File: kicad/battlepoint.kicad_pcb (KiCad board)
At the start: 2 copper layers, 13 parts, among them J1 Arduino1, J2 Arduino2, J3 Arduino3, J4 Arduino4, J5 PANEL, J6 SWITCHES, J7 Barrel_Jack, J8 LIGHTS, U1 LM7805_TO220

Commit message: working mostly
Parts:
- removed C1: 0.1uf, Capacitors_THT:C_Rect_L7.0mm_W2.5mm_P5.00mm
- removed C2: 22uf, Capacitors_THT:CP_Radial_D4.0mm_P1.50mm
- removed J2: Arduino2, Socket_Strips:Socket_Strip_Straight_1x06_Pitch2.54mm
- removed J3: Arduino3, Socket_Strips:Socket_Strip_Straight_1x08_Pitch2.54mm
- removed J4: Arduino4, Socket_Strips:Socket_Strip_Straight_1x08_Pitch2.54mm
- removed J5: PANEL, Connectors:RJ45_8
- removed J6: SWITCHES, Connectors:RJ45_8
- removed J7: Barrel_Jack, Connectors:BARREL_JACK
- removed J8: LIGHTS, Connectors:RJ45_8
- added ARD1: UNO_SHIELD, Arduino:Arduino_Uno_Shield, F.Cu at (87.6, 188.0)
- added P1: TMR1_LED, Connect:USB_A, F.Cu at (74.9, 99.1)
- added P10: OLED, Connectors_JST:JST_XH_B04B-XH-A_04x2.50mm_Straight, F.Cu at (47.0, 143.5)
- added P2: TMR2_LED, Connect:USB_A, F.Cu at (40.6, 99.1)
- added P3: CAP_LED, Connect:USB_A, F.Cu at (58.4, 99.1)
- added P4: OWN_LED, Connect:USB_A, F.Cu at (91.4, 99.1)
- added P5: SPK, Connectors_JST:JST_XH_B02B-XH-A_02x2.50mm_Straight, F.Cu at (68.6, 130.8)
- added P8: AUDIO_JACK, Connectors_JST:JST_XH_B04B-XH-A_04x2.50mm_Straight, F.Cu at (47.0, 129.5)
- added P9: KEYPAD, Connectors_JST:JST_XH_B03B-XH-A_03x2.50mm_Straight, F.Cu at (63.5, 143.5)
- J1: value Arduino1 -> BTNS; footprint Socket_Strips:Socket_Strip_Straight_1x06_Pitch2.54mm -> Connect:RJ45_8
- R1, R2: footprint Resistors_THT:R_Axial_DIN0204_L3.6mm_D1.6mm_P2.54mm_Vertical -> Resistors_ThroughHole:Resistor_Horizontal_RM7mm
- U1: value LM7805_TO220 -> DFPLAYER_MINI; footprint TO_SOT_Packages_THT:TO-220-3_Vertical -> Arduino:dfplayer_mini
- moved R2 77.2 mm to (80.0, 149.9)
- moved U1 74.7 mm to (45.7, 156.2)
- moved R1 72.9 mm to (80.0, 137.2)
- moved J1 55.7 mm to (41.9, 110.5), turned to 90 degrees
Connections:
- J1 pad 1: A5 -> GND
- J1 pad 2: A4 -> +5V
- J1 pad 3: A3 -> D2
- J1 pad 4: A2 -> D11
- J1 pad 5: A1 -> GND
- J1 pad 6: A0 -> +5V
- R1 pad 1: +VDC -> Net-(ARD1-PadVIN)
- R1 pad 2: A2 -> A4
- R2 pad 1: A2 -> A4
- R2 pad 2: Net-(J7-Pad2) -> GND
- U1 pad 1: +VDC -> +5V
- U1 pad 2: GND -> D8
- U1 pad 3: +5V -> D9
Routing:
- net A2: track 112.0 -> 0.00 mm
- net GND: track 91.9 -> 0.00 mm
- net A0: track 44.5 -> 0.00 mm
- net P3: track 36.2 -> 0.00 mm
- net +VDC: track 32.6 -> 0.00 mm
- net P5: track 32.1 -> 0.00 mm
- net +5V: track 31.8 -> 0.00 mm
- net P6: track 31.3 -> 0.00 mm
- net A4: track 18.1 -> 0.00 mm
- net A5: track 12.5 -> 0.00 mm
- net Net-(J7-Pad2): track 9.03 -> 0.00 mm
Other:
- board outline added: 77.5 x 100.3 mm
- net class PWR removed

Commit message: progress
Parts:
- removed P10: OLED, Connectors_JST:JST_XH_B04B-XH-A_04x2.50mm_Straight
- removed P9: KEYPAD, Connectors_JST:JST_XH_B03B-XH-A_03x2.50mm_Straight
- added P12: PANEL_OUT, Connectors_JST:JST_XH_B05B-XH-A_05x2.50mm_Straight, F.Cu at (109.2, 184.2)
- added P13: PANEL_IN, Connectors_JST:JST_XH_B05B-XH-A_05x2.50mm_Straight, F.Cu at (66.0, 100.3)
- added P14: OLED_OUT, Connectors_JST:JST_XH_B04B-XH-A_04x2.50mm_Straight, F.Cu at (91.4, 95.2)
- added R3: 2K, Resistors_ThroughHole:Resistor_Horizontal_RM7mm, F.Cu at (26.7, 92.7)
- added R4: 330, Resistors_ThroughHole:Resistor_Horizontal_RM7mm, F.Cu at (39.4, 92.7)
- added R5: 620, Resistors_ThroughHole:Resistor_Horizontal_RM7mm, F.Cu at (52.1, 92.7)
- added R6: 1K, Resistors_ThroughHole:Resistor_Horizontal_RM7mm, F.Cu at (63.5, 92.7)
- added R7: 3.3K, Resistors_ThroughHole:Resistor_Horizontal_RM7mm, F.Cu at (74.9, 92.7)
- added SW1: BTN_UP, Buttons_Switches_ThroughHole:SW_PUSH_6mm, B.Cu at (26.7, 97.8)
- added SW2: BTN_DWN, Buttons_Switches_ThroughHole:SW_PUSH_6mm, B.Cu at (39.4, 97.8)
- added SW3: BTN_SEL, Buttons_Switches_ThroughHole:SW_PUSH_6mm, B.Cu at (52.1, 97.8)
- moved P8 71.7 mm to (109.2, 165.1), turned to 90 degrees
- moved J1 63.7 mm to (105.4, 115.6), turned to 180 degrees
- moved P2 55.2 mm to (91.4, 120.7)
- moved P5 45.8 mm to (101.6, 162.6), turned to 270 degrees
- moved P3 30.5 mm to (36.8, 120.7)
- moved P1 28.8 mm to (55.9, 120.7)
- moved P4 28.0 mm to (73.7, 120.7)
- moved U1 15.2 mm to (45.7, 171.4)
- moved R1 13.7 mm to (87.6, 148.6)
- moved R2 11.7 mm to (87.6, 158.8)
- moved ARD1 8.13 mm to (82.5, 194.3)
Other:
- board size 77.5 x 100.3 mm -> 101.6 x 153.7 mm

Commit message: about to start routing
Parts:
- R3, R4, R5, R6, R7: footprint Resistors_ThroughHole:Resistor_Horizontal_RM7mm -> Resistors_ThroughHole:Resistor_Vertical_RM5mm
- moved P12 39.4 mm to (109.2, 144.8)
- moved P14 38.9 mm to (53.3, 102.9), turned to 180 degrees
- moved R3 36.1 mm to (61.0, 104.1), turned to 180 degrees
- moved P13 28.1 mm to (38.1, 102.9), turned to 180 degrees
- moved U1 25.7 mm to (59.7, 149.9)
- moved R4 22.9 mm to (61.0, 100.3), turned to 180 degrees
- moved R7 14.5 mm to (61.0, 88.9), turned to 180 degrees
- moved ARD1 14.0 mm to (96.5, 194.3)
- moved P5 14.0 mm to (101.6, 176.5)
- moved P8 14.0 mm to (109.2, 179.1)
- moved R2 13.3 mm to (100.3, 162.6)
- moved R1 13.0 mm to (100.3, 151.1)
- moved R5 9.67 mm to (61.0, 96.5), turned to 180 degrees
- moved SW3 8.52 mm to (48.3, 90.2)
- moved SW1 8.52 mm to (30.5, 90.2)
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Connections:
- ARD1 pad SCL: Net-(ARD1-PadSCL) -> SCL
- ARD1 pad SDA: Net-(ARD1-PadSDA) -> SDA
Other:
- net class Default: clearance 0.2 -> 0.3; trace_width 0.25 -> 0.4
- net class PWR added: clearance 0.3, trace_width 0.5, via_dia 0.6, via_drill 0.4
- rule trace_clearance: 0.2 -> 0.3

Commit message: finished for now i think
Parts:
- moved P3 72.4 mm to (109.2, 120.7)
- moved J1 72.4 mm to (33.0, 115.6)
- moved P12 66.0 mm to (52.1, 177.8)
- moved P1 35.6 mm to (91.4, 120.7)
- moved P4 20.3 mm to (53.3, 120.7)
- moved P2 19.0 mm to (72.4, 120.7)
- moved P14 16.6 mm to (36.8, 101.6)
- moved P13 15.3 mm to (53.3, 101.6)
- moved R7 1.27 mm to (61.0, 87.6)
- moved R3 1.27 mm to (61.0, 102.9)
- moved R4 1.27 mm to (61.0, 99.1)
- moved R5 1.27 mm to (61.0, 95.2)
- moved R6 1.27 mm to (61.0, 91.4)
- moved SW1 1.27 mm to (30.5, 88.9)
- moved SW2 1.27 mm to (39.4, 88.9)
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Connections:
- ARD1 pad A4: Net-(ARD1-PadA4) -> A4
- P8 pad 4: Net-(P8-Pad4) -> Net-(P8-Pad2)
- U1 pad 6: Net-(P8-Pad4) -> Net-(P8-Pad2)
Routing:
- net GND: track 0.00 -> 481.0 mm
- net +5V: track 0.00 -> 331.9 mm
- net Net-(P8-Pad2): track 0.00 -> 121.1 mm
- net D5: track 0.00 -> 112.1 mm
- net Net-(P5-Pad1): track 0.00 -> 105.3 mm
- net A0: track 0.00 -> 93.7 mm
- net D11: track 0.00 -> 73.5 mm
- net D10: track 0.00 -> 65.5 mm
- net A4: track 0.00 -> 64.7 mm
- net Net-(R4-Pad2): track 0.00 -> 51.8 mm
- net Net-(P1-Pad3): track 0.00 -> 38.2 mm
- net Net-(P2-Pad3): track 0.00 -> 38.2 mm
- net Net-(P1-Pad2): track 0.00 -> 36.4 mm
- net D3: track 0.00 -> 36.2 mm
- net Net-(R5-Pad2): track 0.00 -> 27.9 mm
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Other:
- board size 101.6 x 153.7 mm -> 101.6 x 154.9 mm
- net class Default: trace_width 0.4 -> 0.6
- net class PWR: trace_width 0.5 -> 0.8

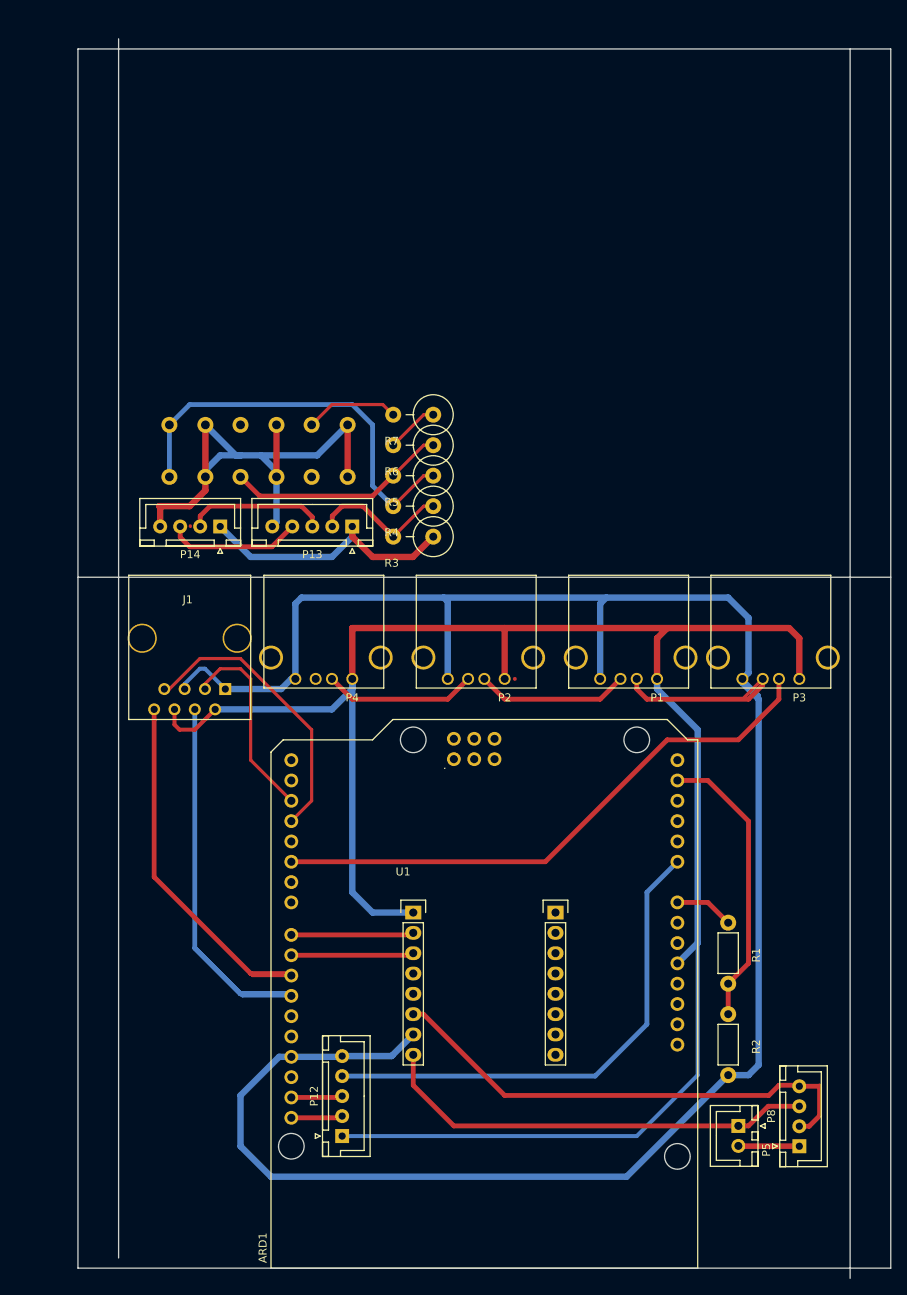
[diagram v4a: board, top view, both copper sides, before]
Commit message: used rj45s for connections
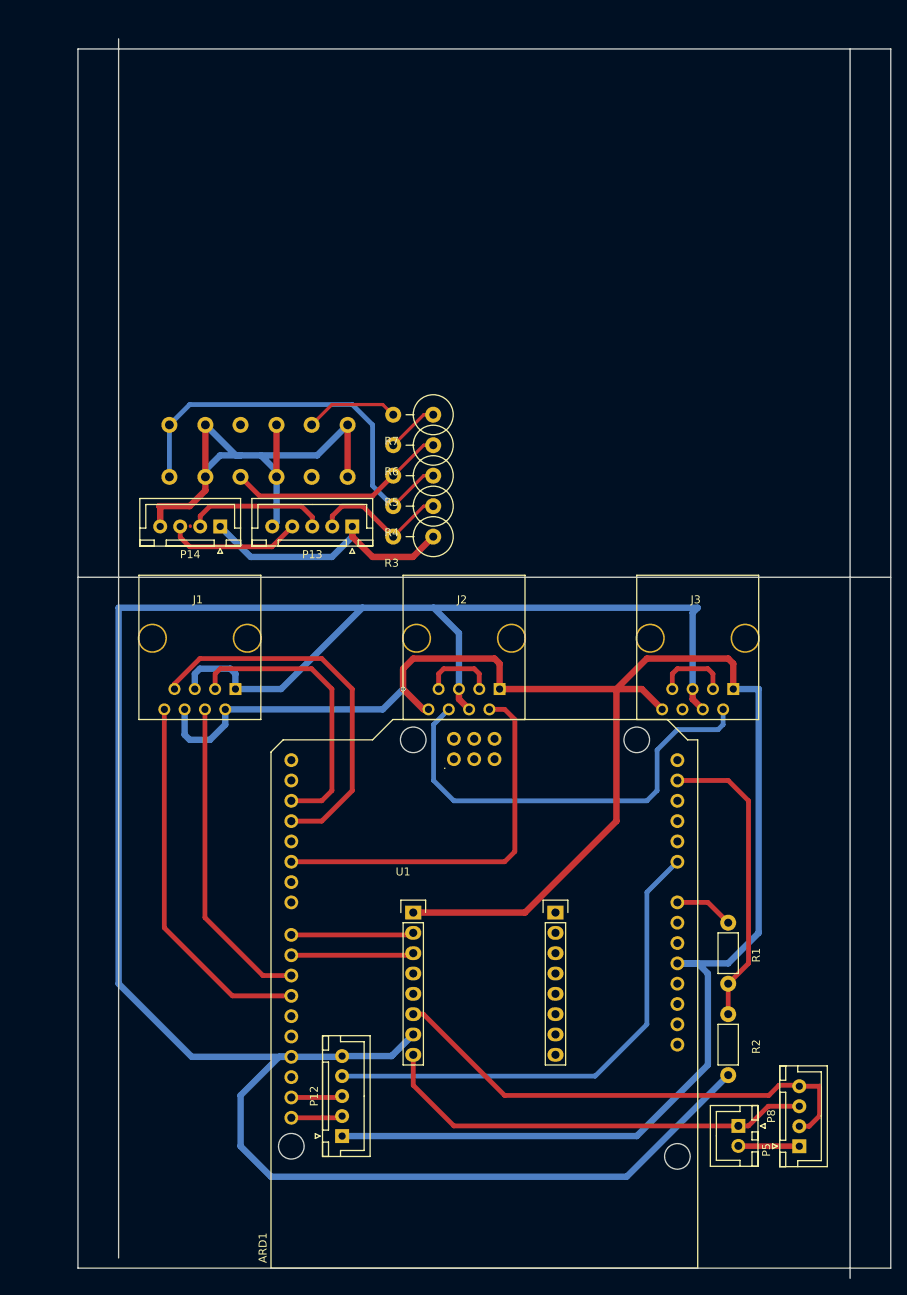
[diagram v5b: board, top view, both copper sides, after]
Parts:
- removed P1: TMR1_LED, Connect:USB_A
- removed P2: TMR2_LED, Connect:USB_A
- removed P3: CAP_LED, Connect:USB_A
- removed P4: OWN_LED, Connect:USB_A
- added J2: TMR_LEDS, Connect:RJ45_8, F.Cu at (67.3, 115.6)
- added J3: CAP_LEDS, Connect:RJ45_8, F.Cu at (96.5, 115.6)
- moved J1 1.27 mm to (34.3, 115.6)
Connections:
- J1 pad 4: D11 -> D10
- J1 pad 8: D10 -> D11
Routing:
- net D5: track 112.1 -> 48.7 mm
- net Net-(J2-Pad6): track 0.00 -> 55.8 mm
- net +5V: track 331.9 -> 289.4 mm, vias 0 -> 1
- net Net-(P1-Pad3): track 38.2 -> 0.00 mm
- net Net-(P2-Pad3): track 38.2 -> 0.00 mm
- net Net-(P1-Pad2): track 36.4 -> 0.00 mm
- net GND: track 481.0 -> 454.6 mm
- net D11: track 73.5 -> 47.4 mm
- net D10: track 65.5 -> 40.2 mm
- net A4: track 64.7 -> 41.3 mm
- net D3: track 36.2 -> 47.7 mm
- net D2: track 25.0 -> 36.1 mm
- net Net-(J3-Pad3): track 0.00 -> 9.42 mm
- net Net-(J2-Pad3): track 0.00 -> 9.42 mm
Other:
- net class SMALL added: clearance 0.3, trace_width 0.3, via_dia 0.6, via_drill 0.4

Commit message: moved stuff
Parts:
- moved R3 2.54 mm to (61.0, 100.3)
- moved R4 2.54 mm to (61.0, 96.5)
- moved R5 2.54 mm to (61.0, 92.7)
- moved SW1 2.54 mm to (30.5, 86.4)
- moved SW2 2.54 mm to (39.4, 86.4)
- moved SW3 2.54 mm to (48.3, 86.4)
- moved R6 2.54 mm to (61.0, 88.9)
- moved R7 2.54 mm to (61.0, 85.1)
- moved P13 1.27 mm to (53.3, 100.3)
- moved P14 1.27 mm to (36.8, 100.3)
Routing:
- net GND: track 454.6 -> 457.1 mm
- net +5V: track 289.4 -> 287.8 mm
- net Net-(P13-Pad3): track 17.6 -> 19.1 mm

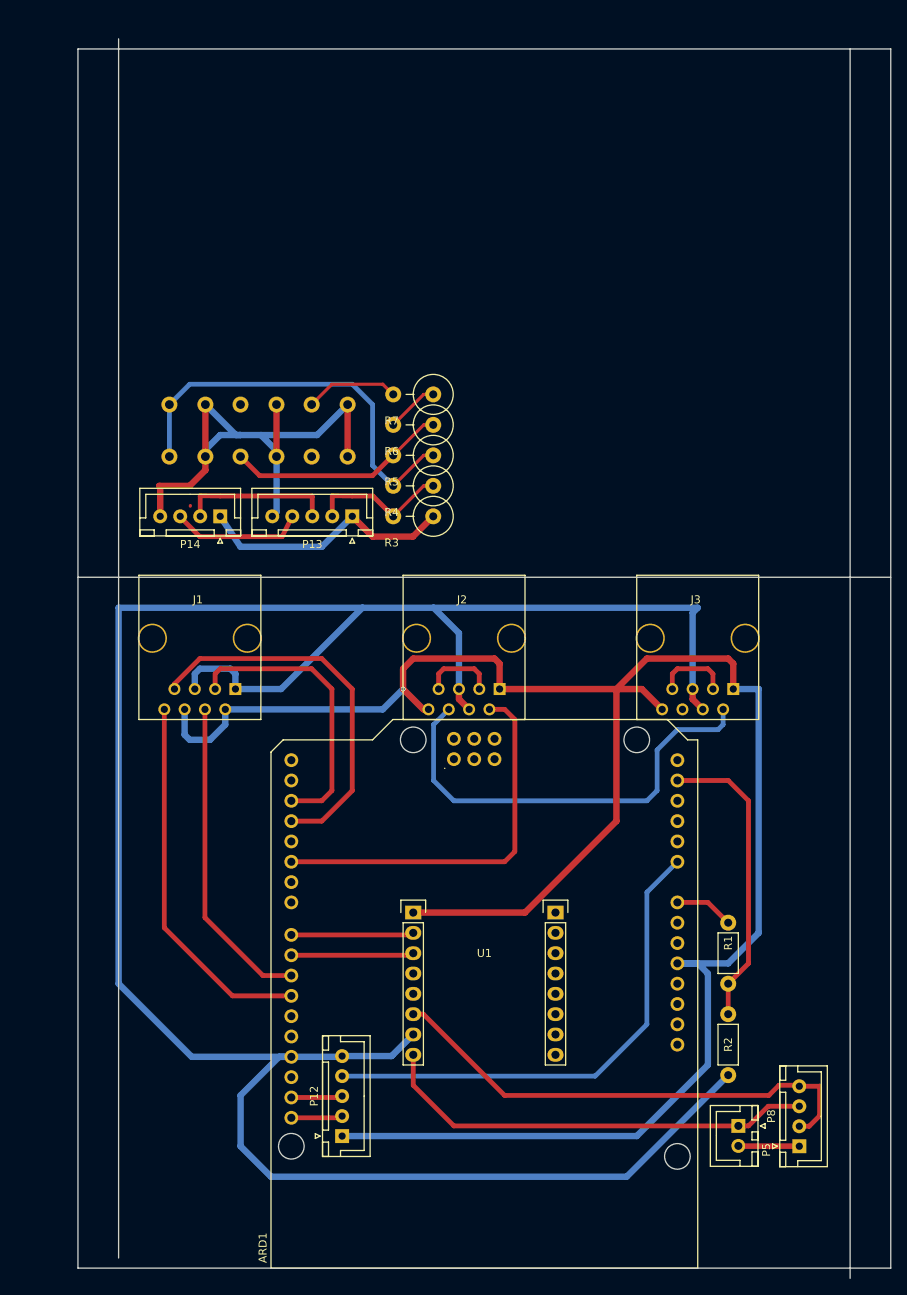
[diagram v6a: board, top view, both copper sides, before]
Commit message: more compact layout
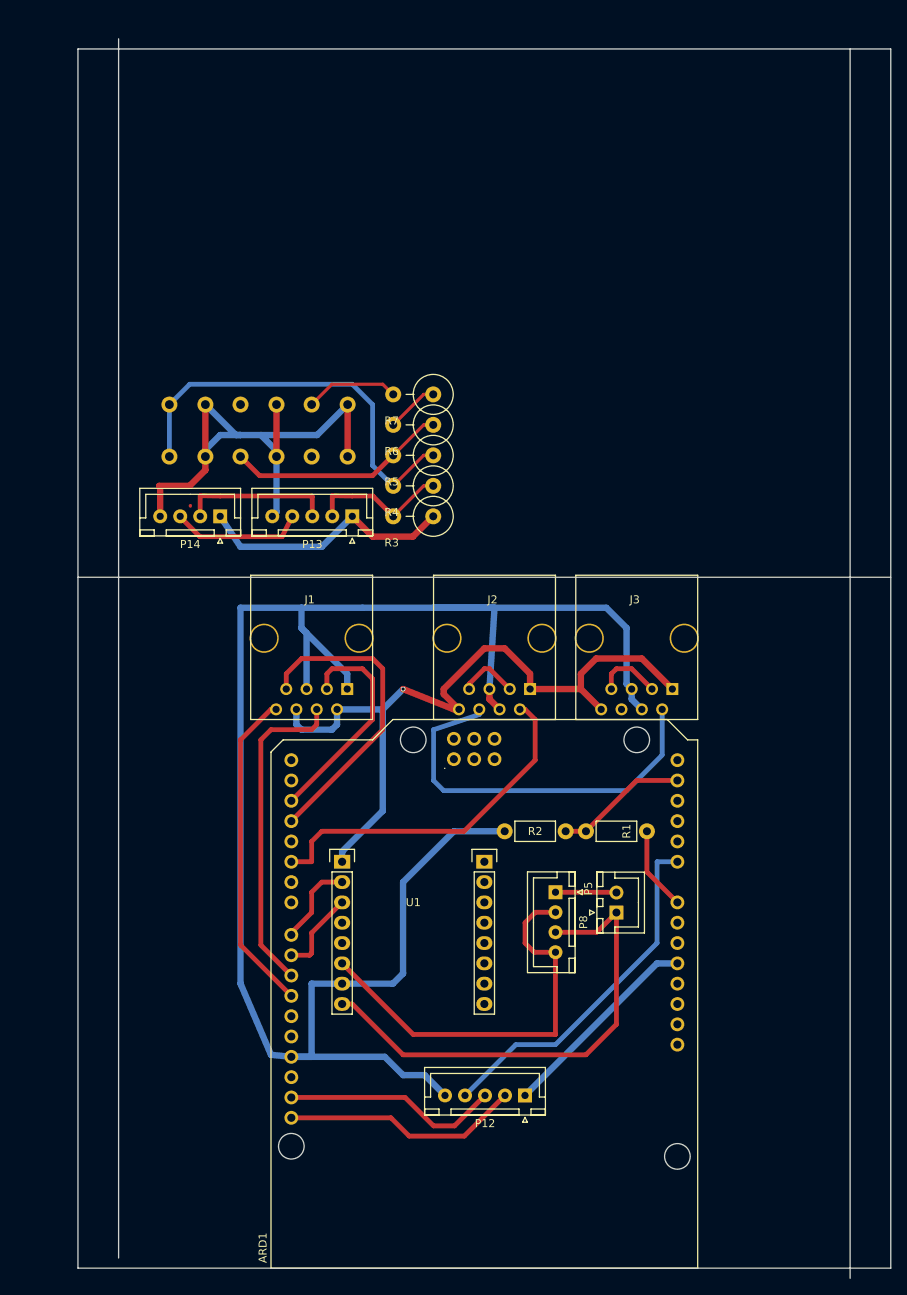
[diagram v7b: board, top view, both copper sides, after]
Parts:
- moved P8 44.0 mm to (78.7, 147.3), turned to 270 degrees
- moved P5 30.7 mm to (86.4, 149.9), turned to 90 degrees
- moved R2 30.6 mm to (80.0, 139.7), turned to 180 degrees
- moved P12 23.4 mm to (74.9, 172.7), turned to 180 degrees
- moved R1 15.3 mm to (90.2, 139.7), turned to 180 degrees
- moved J1 14.0 mm to (48.3, 115.6)
- moved U1 10.9 mm to (50.8, 143.5)
- moved J3 7.62 mm to (88.9, 115.6)
- moved J2 3.81 mm to (71.1, 115.6)
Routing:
- net GND: track 457.1 -> 303.9 mm
- net +5V: track 287.8 -> 150.7 mm
- net Net-(P8-Pad2): track 121.1 -> 51.8 mm
- net A0: track 93.7 -> 44.6 mm
- net Net-(P5-Pad1): track 105.3 -> 61.1 mm
- net A4: track 41.3 -> 16.6 mm
- net SCL: track 7.04 -> 30.1 mm
- net SDA: track 6.91 -> 27.5 mm
- net D3: track 47.7 -> 39.1 mm
- net D2: track 36.1 -> 27.9 mm
- net Net-(P5-Pad2): track 15.3 -> 7.64 mm
- net Net-(J2-Pad6): track 55.8 -> 49.7 mm
- net D11: track 47.4 -> 41.4 mm
- net D9: track 15.7 -> 10.6 mm
- net D8: track 15.7 -> 10.7 mm
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
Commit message: more compact layout
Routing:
- net +5V: track 150.7 -> 187.7 mm
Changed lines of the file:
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@@
   (general
     (links 62)
-    (no_connects 5)
+    (no_connects 4)
     (area 18.974999 40.564999 120.725001 201.035001)
     (thickness 1.6)
     (drawings 7)
-    (tracks 226)
+    (tracks 230)
     (zones 0)
     (modules 20)
@@
   (segment (start 90.17 139.7) (end 90.17 144.78) (width 0.6) (layer F.Cu) (net 7))
   (segment (start 90.17 144.78) (end 93.98 148.59) (width 0.6) (layer F.Cu) (net 7))
+  (segment (start 93.345 121.92) (end 93.98 121.92) (width 0.8) (layer F.Cu) (net 10) (status C00000))
+  (segment (start 93.98 121.92) (end 96.52 124.46) (width 0.8) (layer F.Cu) (net 10) (status 400000))
+  (segment (start 96.52 153.67) (end 93.98 156.21) (width 0.8) (layer F.Cu) (net 10) (status 800000))
+  (segment (start 96.52 124.46) (end 96.52 153.67) (width 0.8) (layer F.Cu) (net 10))
   (segment (start 75.565 121.92) (end 75.565 120.015) (width 0.8) (layer F.Cu) (net 10) (status 400000))
   (segment (start 64.77 122.555) (end 66.675 124.46) (width 0.8) (layer F.Cu) (net 10) (status 800000))
